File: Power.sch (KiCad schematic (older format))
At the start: 42 parts, among them J5 GS2, J6 XT60-M, U12 TL1963A-33DCYR, U13 INA181AX, U14 LM2931, U15 INA181AX, U16 MCP1501

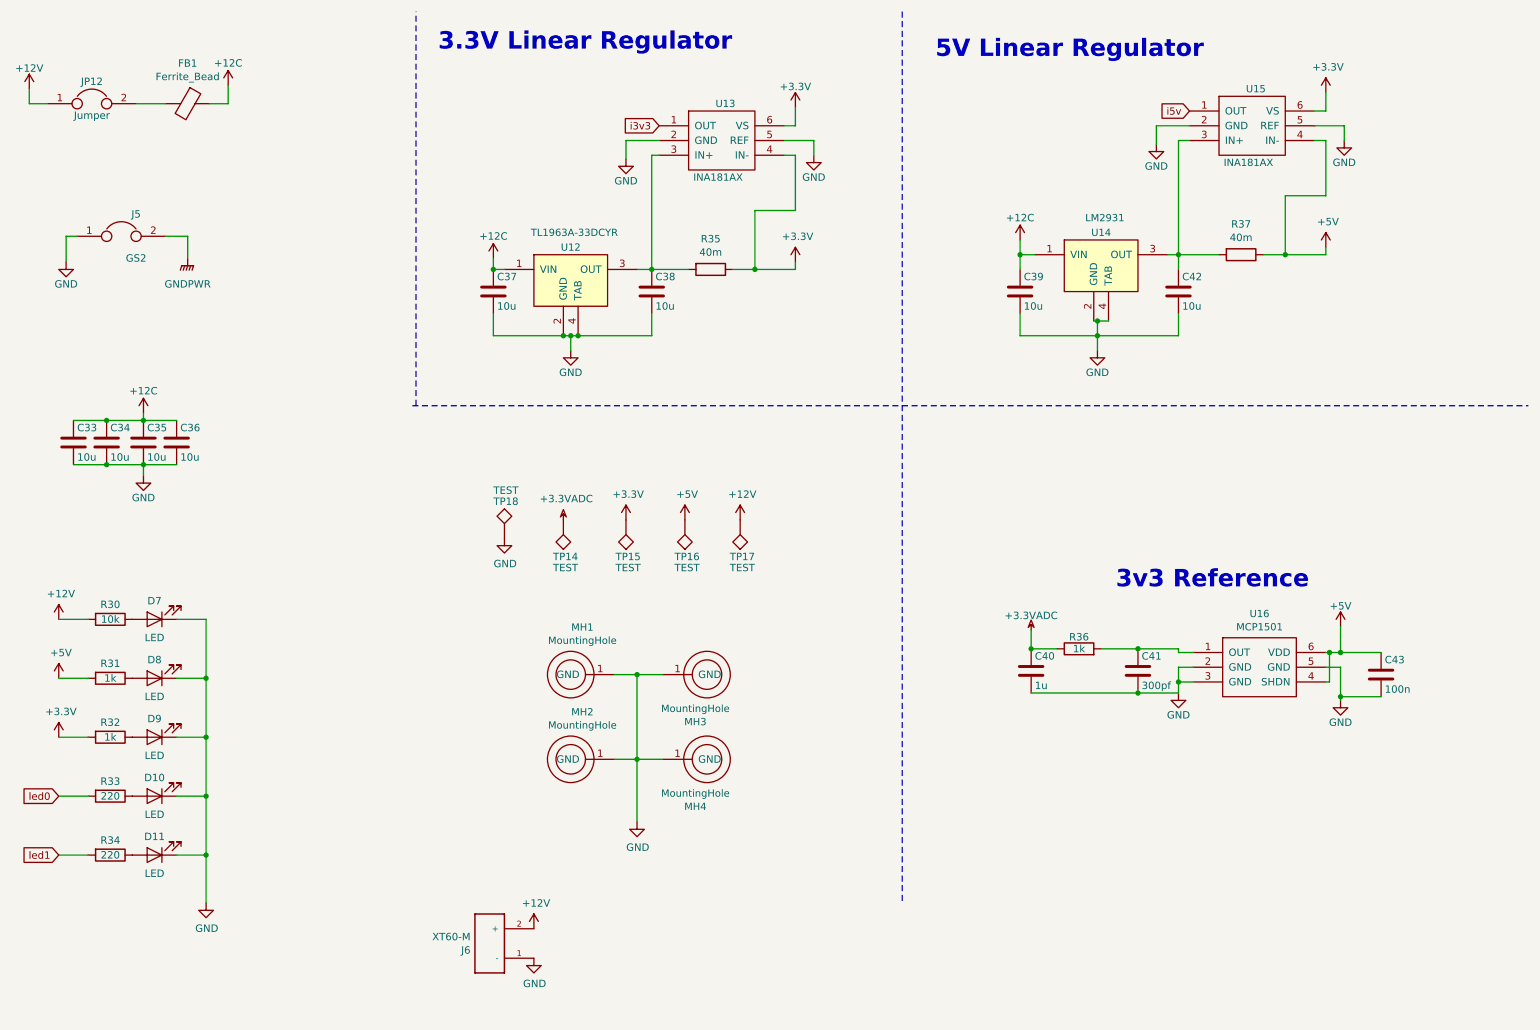
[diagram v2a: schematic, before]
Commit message: Motor Channel Cleanup
Removed some leftover labels in the motor channel after removal of the AND gate. Renumbering.
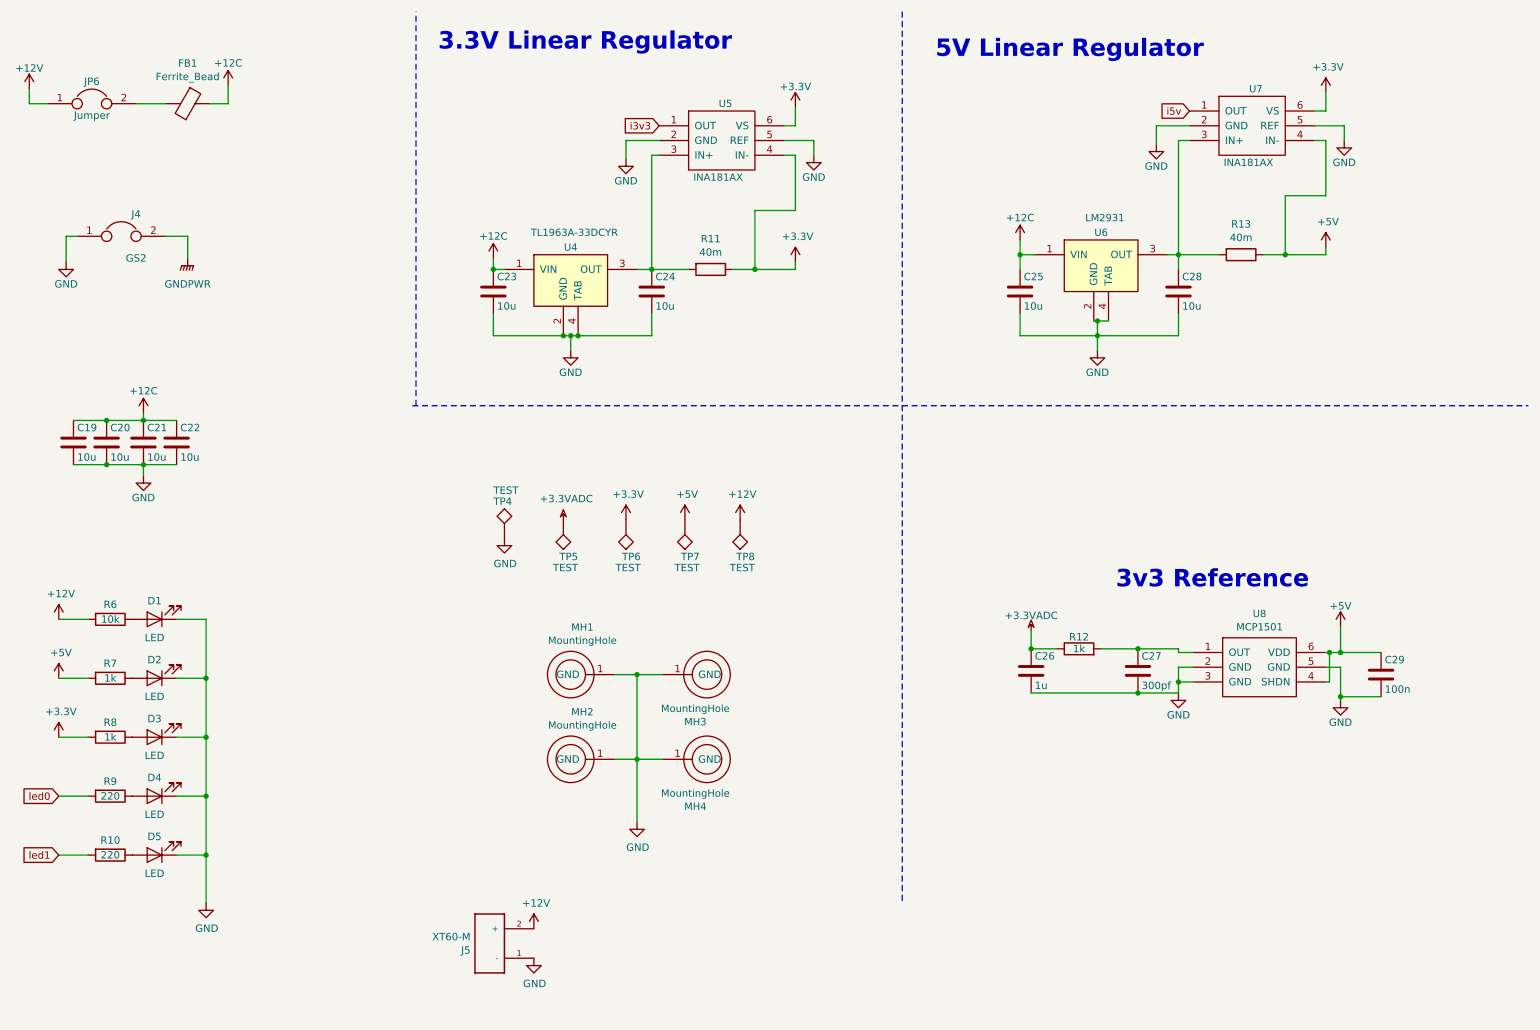
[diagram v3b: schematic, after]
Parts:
- renumbered C33 to C19, C34 to C20, C35 to C21, C36 to C22, C37 to C23, C38 to C24, C39 to C25, C40 to C26, C41 to C27, C42 to C28, C43 to C29, D7 to D1, D8 to D2, D9 to D3, D10 to D4, D11 to D5, J5 to J4, J6 to J5, JP12 to JP6, R34 to R10, R35 to R11, R36 to R12, R37 to R13, R30 to R6, R31 to R7, R32 to R8, R33 to R9, TP18 to TP4, TP14 to TP5, TP15 to TP6, TP16 to TP7, TP17 to TP8, U12 to U4, U13 to U5, U14 to U6, U15 to U7, U16 to U8
